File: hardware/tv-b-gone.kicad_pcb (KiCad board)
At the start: 2 copper layers, 50 x 35 mm, 18 parts, among them J1 USB_C_Receptacle_PowerOnly_6P, Q1 2N7000, SW1 SW_Push, U1 ATtiny85-20P

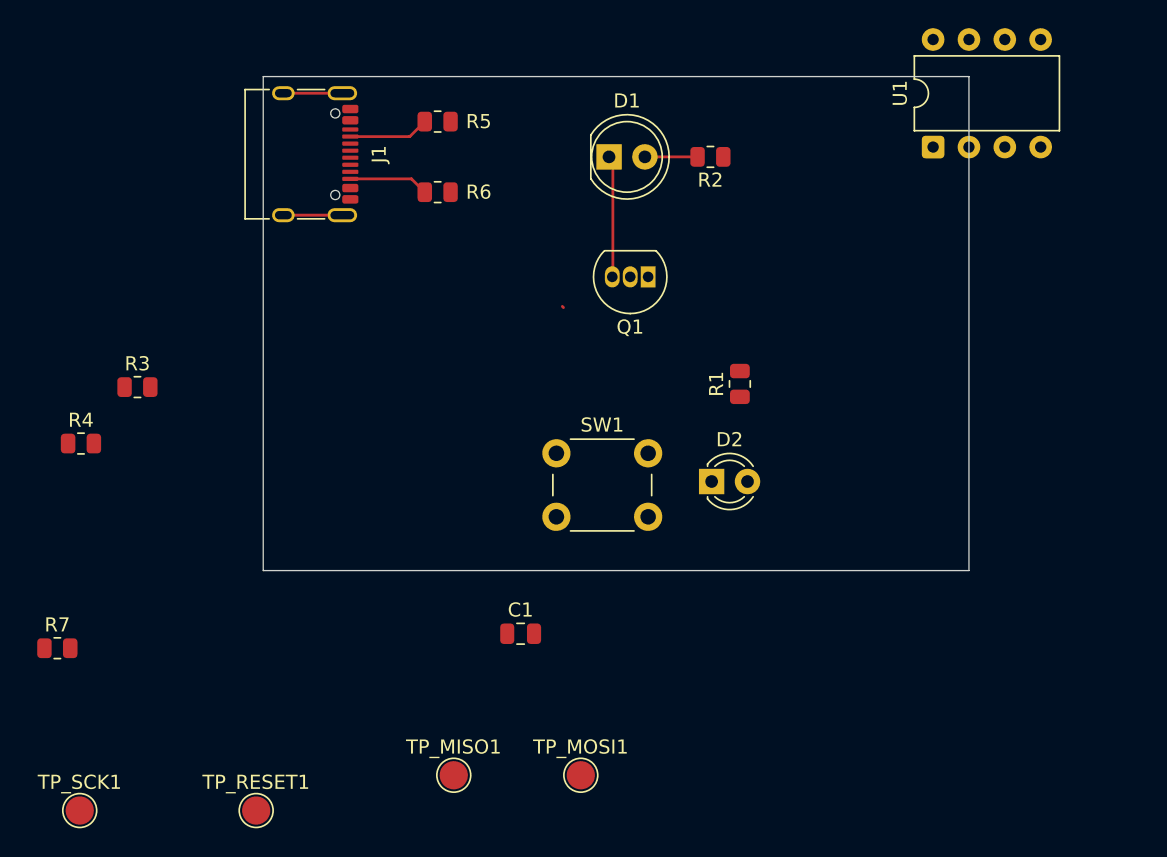
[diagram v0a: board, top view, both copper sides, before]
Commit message: PCB power test points connected
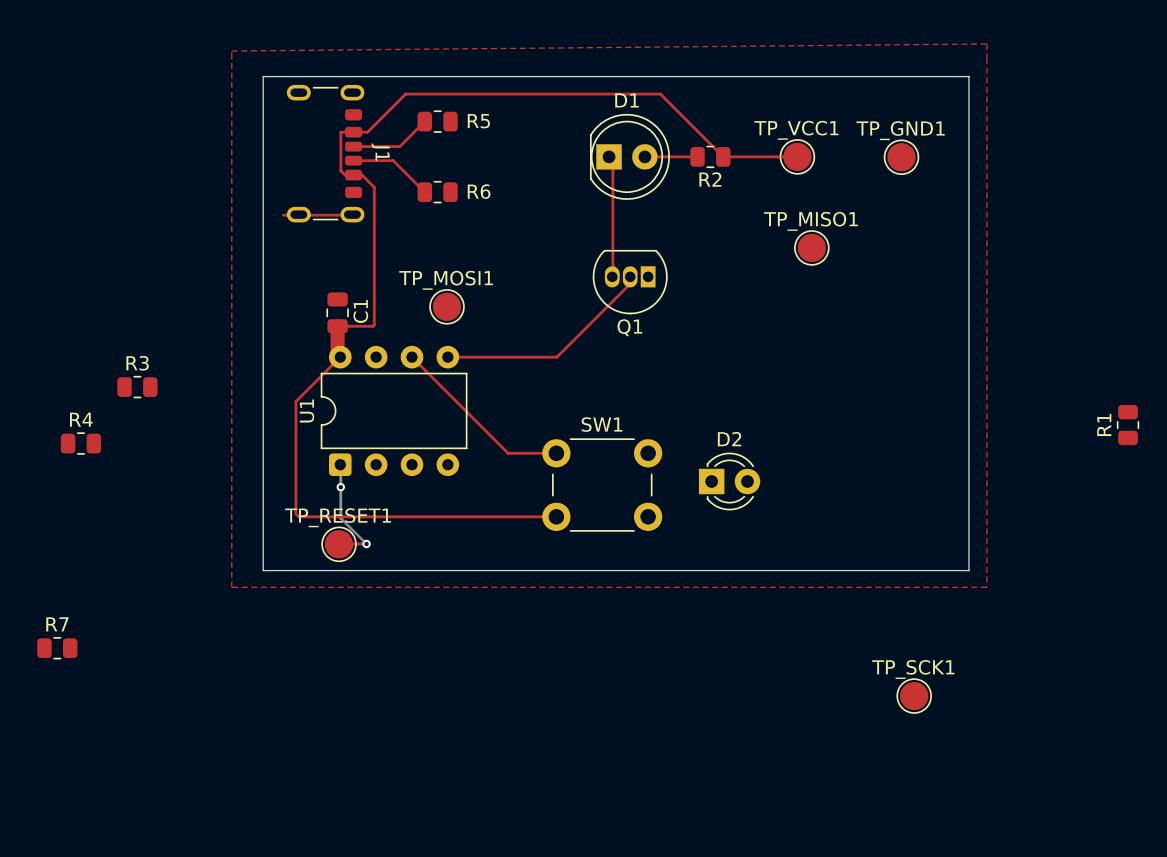
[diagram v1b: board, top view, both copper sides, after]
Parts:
- added TP_GND1: TestPoint, TestPoint:TestPoint_Pad_D2.0mm, F.Cu at (186.9, 85.0)
- added TP_VCC1: TestPoint, TestPoint:TestPoint_Pad_D2.0mm, F.Cu at (179.6, 85.0)
- J1: footprint Connector_USB:USB_C_Receptacle_XKB_U262-16XN-4BVC11 -> Connector_USB:USB_C_Receptacle_GCT_USB4125-xx-x-0190_6P_TopMnt_Horizontal
- moved TP_SCK1 59.7 mm to (187.8, 123.2)
- moved U1 47.6 mm to (147.2, 106.8)
- moved TP_MISO1 45.2 mm to (180.6, 91.5)
- moved TP_MOSI1 34.5 mm to (154.8, 95.6)
- moved R1 27.7 mm to (203.0, 104.0)
- moved C1 26.2 mm to (147.0, 96.0), turned to -90 degrees
- moved TP_RESET1 19.8 mm to (147.1, 112.5)
- moved J1 0.82 mm to (145.1, 84.8)
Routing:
- net +5V: track 0.00 -> 86.5 mm
- net Net-(Q1-G): track 0.00 -> 15.6 mm
- net Net-(U1-PB1): track 0.00 -> 13.1 mm
- net Net-(U1-~{RESET}/PB5): track 0.11 -> 8.35 mm, vias 0 -> 2
- net GND: track 8.36 -> 4.18 mm
- added copper zone on F.Cu, net GND

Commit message: PCB finished
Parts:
- moved R7 52.0 mm to (176.1, 102.4), turned to 90 degrees
- moved R1 48.8 mm to (154.8, 111.5), turned to 180 degrees
- moved R3 44.7 mm to (176.1, 89.9), turned to 90 degrees
- moved R4 40.4 mm to (169.0, 101.5), turned to 90 degrees
- moved TP_SCK1 38.5 mm to (160.9, 95.7)
- moved TP_MISO1 21.1 mm to (162.6, 102.4)
- moved TP_GND1 7.57 mm to (181.0, 89.7)
- moved TP_VCC1 1.43 mm to (181.0, 85.0)
- moved TP_RESET1 1.11 mm to (146.1, 112.0)
- moved TP_MOSI1 0.93 mm to (153.8, 95.7)
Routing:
- net Net-(U1-XTAL1/PB3): track 0.00 -> 30.8 mm, vias 0 -> 1
- net Net-(U1-PB2): track 0.00 -> 17.2 mm
- net GND: track 4.18 -> 20.6 mm, vias 0 -> 2
- net Net-(Q1-G): track 15.6 -> 30.0 mm
- net Net-(U1-PB1): track 13.1 -> 26.7 mm
- net +5V: track 86.5 -> 96.9 mm
- net Net-(U1-~{RESET}/PB5): track 8.35 -> 14.8 mm, vias 2 -> 1
- net Net-(D2-A): track 0.00 -> 4.74 mm
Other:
- board size 50 x 35 mm -> 43.1 x 35 mm
